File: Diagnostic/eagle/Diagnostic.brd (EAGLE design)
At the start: 90.2 x 80.9 mm, 70 parts, among them J1 S7036-ND, J2 S7036-ND, J3 1175-1864-ND, J4 503182-1852, J5 277-1578-ND, Q1 16 MHz, Q2 16MHz, T2 LD1086D2M33TR, U1 ATMEGA2560AU, U2 BME280, U3 ATMEGA328P-AUR, U4 TXB0108PWR, U5 TPS565208DDCR, U6 TXB0108PWR, X1 B6B-EH-A(LF)(SN), X3 NRF24L01, X5 1751248

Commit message: Working on the board
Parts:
- moved X3 170.1 mm to (44.5, 10.2), turned to 180 degrees
- moved R7 158.3 mm to (73.7, 63.5), turned to 270 degrees
- moved J2 153.0 mm to (87.6, 64.8), turned to 90 degrees
- moved R3 144.5 mm to (71.1, 63.5), turned to 270 degrees
- moved R5 144.0 mm to (64.8, 100.3)
- moved J1 143.1 mm to (87.6, 73.7), turned to 90 degrees
- moved U1 123.9 mm to (47.0, 40.6)
- moved J3 120.9 mm to (83.8, 55.9)
- moved C8 105.4 mm to (59.7, 61.0), turned to 270 degrees
- moved U3 101.4 mm to (73.7, 72.4)
- moved C7 96.8 mm to (59.7, 76.2), turned to 90 degrees
- moved J4 95.6 mm to (10.2, 10.2)
- moved FUSE 89.0 mm to (52.1, 73.7), turned to 180 degrees
- moved U6 86.4 mm to (44.5, 14.0)
- moved C9 85.1 mm to (63.5, 88.9)
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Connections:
- net +3V3: now also C15.1, T2.2
- net +5V: no longer C15.1, T2.2
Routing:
- net LED_RX_5V: track 0.00 -> 73.8 mm, vias 0 -> 2
- net FAN_PWM: track 0.00 -> 69.0 mm
- net LED_TX_5V: track 0.00 -> 68.9 mm, vias 0 -> 2
- net MOSI1_3V3: track 0.00 -> 65.4 mm, vias 0 -> 2
- net ENCODER_SENSE2: track 0.00 -> 65.0 mm, vias 0 -> 1
- net CON_CONNECTED: track 0.00 -> 65.0 mm
- net MISO1_3V3: track 0.00 -> 64.7 mm
- net ENCODER_SENSE1: track 0.00 -> 62.8 mm, vias 0 -> 1
- net +5V_FUSE: track 0.00 -> 52.9 mm, vias 0 -> 1
- net CURRENT_SENSOR: track 0.00 -> 47.2 mm
- net GND: track 20.6 -> 62.0 mm, vias 2 -> 5
- net SS1_5V: track 0.00 -> 38.8 mm, vias 0 -> 2
- net SS2_5V: track 0.00 -> 37.8 mm, vias 0 -> 2
- net RST: track 0.00 -> 36.5 mm, vias 0 -> 2
- net SS0_3V3: track 0.00 -> 31.4 mm
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- added copper zone on layer 1, net +12V
- added copper zone on layer 1, net +3V3
- added copper zone on layer 1, net +5V
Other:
- board size 90.2 x 80.9 mm -> 90.2 x 82.2 mm

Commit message: Finishing touches with board layout
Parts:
- moved C6 171.7 mm to (82.5, 80.0)
- moved C25 170.2 mm to (82.5, 77.5)
- moved C5 161.5 mm to (78.7, 80.0)
- moved C27 159.0 mm to (80.0, 74.9), turned to 90 degrees
- moved Q1 156.2 mm to (69.8, 38.1), turned to 180 degrees
- moved S3 153.7 mm to (66.0, 61.0)
- moved C4 151.4 mm to (74.9, 80.0)
- moved R1 136.4 mm to (78.7, 33.0)
- moved R10 135.5 mm to (19.8, 2.92), turned to 90 degrees
- moved D1 133.6 mm to (48.3, 76.2)
- moved C2 129.2 mm to (73.7, 33.0)
- moved R9 123.3 mm to (64.6, 31.6)
- moved C19 123.1 mm to (59.1, 20.7)
- moved C24 122.1 mm to (38.1, 53.3)
- moved C23 115.3 mm to (38.1, 55.9)
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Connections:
- net LOGIC_RX_3V3: now also U6.3; no longer U4.1
- net LOGIC_RX_5V: now also U6.18; no longer U4.20
- net LOGIC_TX_3V3: now also U6.1; no longer U4.3
- net LOGIC_TX_5V: now also U6.20; no longer U4.18
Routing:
- net GND: track 62.0 -> 144.6 mm, vias 5 -> 24
- net LS_EN: track 0.00 -> 81.1 mm, vias 0 -> 4
- net !RESET1: track 0.00 -> 55.8 mm, vias 0 -> 2
- net N$3: track 0.00 -> 49.0 mm, vias 0 -> 2
- net LOGIC_RX_3V3: track 0.00 -> 45.1 mm
- net RST: track 36.5 -> 79.4 mm
- net LOGIC_TX_3V3: track 0.00 -> 42.2 mm
- net SD_DETECT_3V3: track 0.00 -> 39.7 mm
- net N$2: track 0.00 -> 36.6 mm, vias 0 -> 2
- net CE_3V3: track 0.00 -> 32.8 mm, vias 0 -> 2
- net SD_DETECT_5V: track 0.00 -> 30.8 mm, vias 0 -> 2
- net SCK1_3V3: track 23.8 -> 53.3 mm, vias 0 -> 4
- net +3V3: track 9.86 -> 37.9 mm, vias 4 -> 5
- net IRQ_5V: track 0.00 -> 27.8 mm, vias 0 -> 2
- net CE_5V: track 5.58 -> 29.3 mm
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
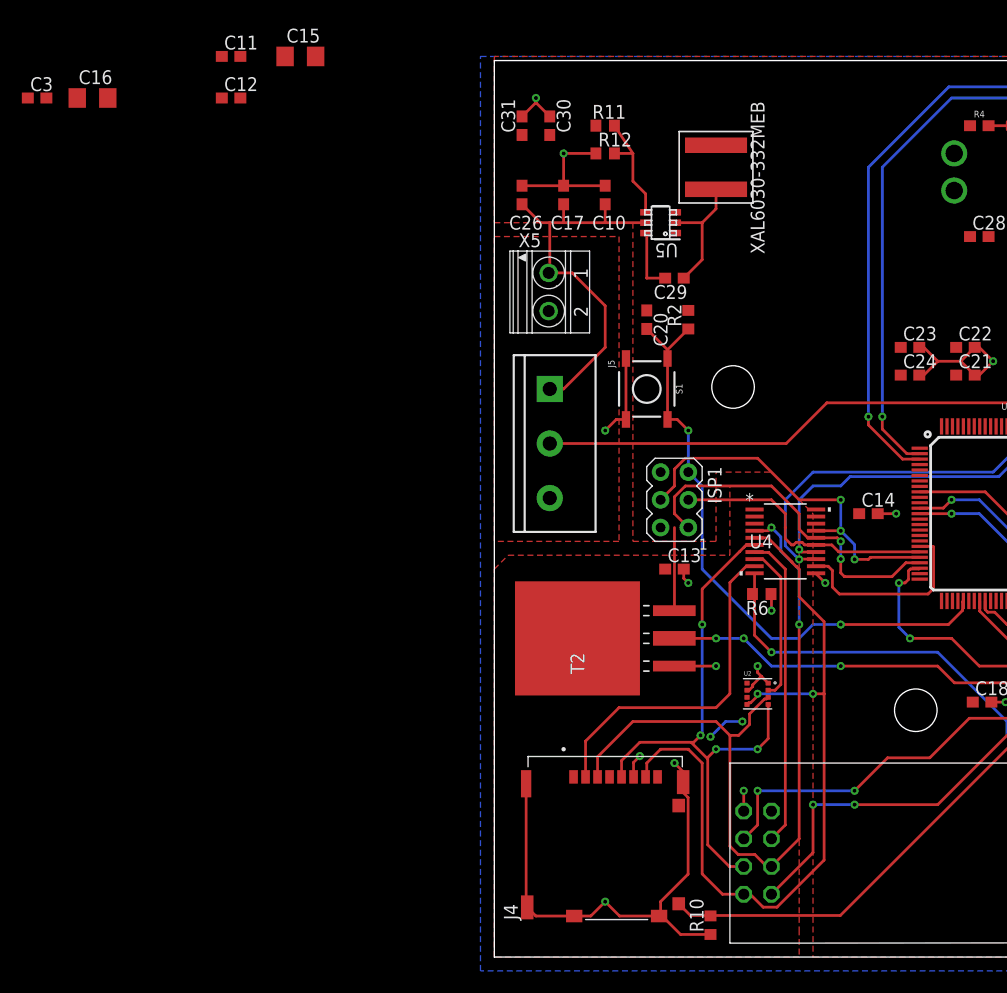
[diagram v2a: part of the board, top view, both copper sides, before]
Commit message: Board functionally done, just need to make it look better
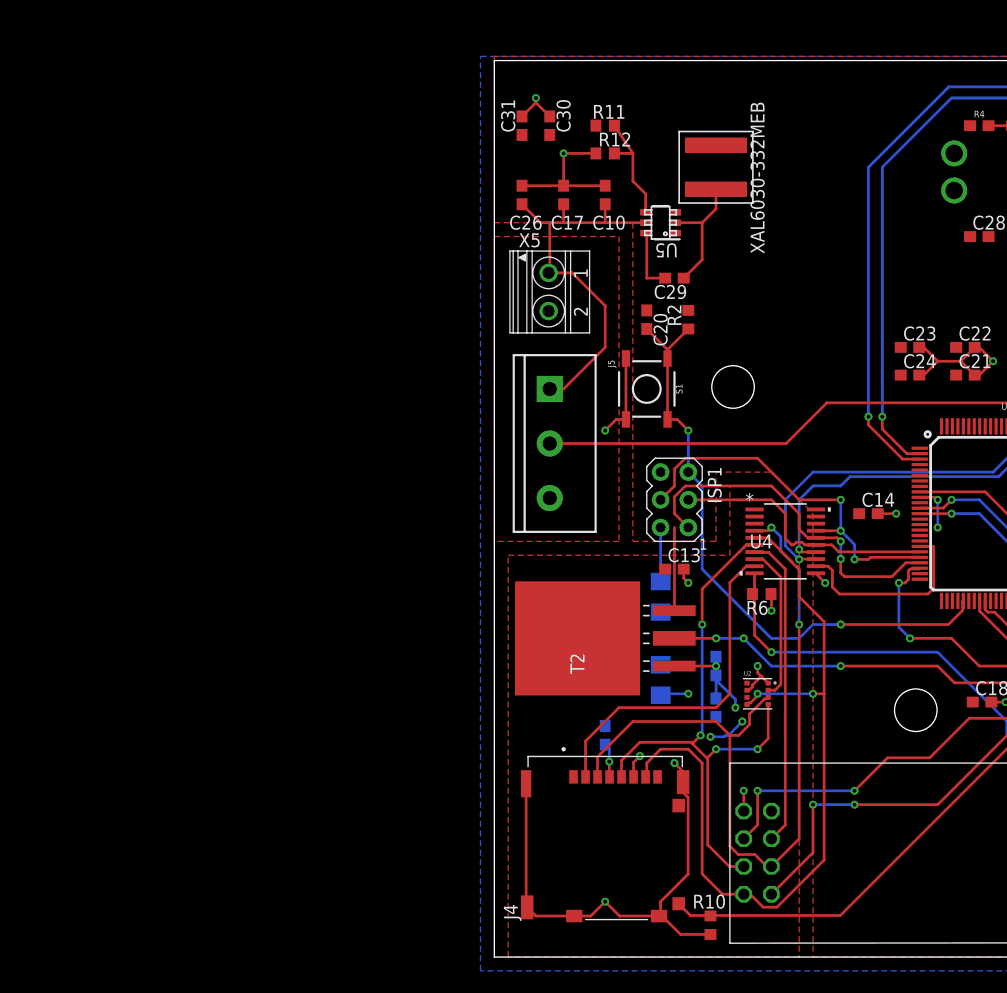
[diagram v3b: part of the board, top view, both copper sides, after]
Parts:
- moved C3 78.3 mm to (10.2, 20.3), flipped to the bottom, turned to 90 degrees
- moved C11 71.4 mm to (20.3, 26.7), flipped to the bottom, turned to 90 degrees
- moved C12 71.4 mm to (20.3, 22.9), flipped to the bottom, turned to 270 degrees
- moved C16 69.3 mm to (15.2, 33.0), flipped to the bottom, turned to 270 degrees
- moved C15 66.0 mm to (15.2, 25.4), flipped to the bottom, turned to 90 degrees
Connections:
- net +3V3: now also C3.1
- net +5V: no longer C3.1
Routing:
- net +3V3: track 37.9 -> 49.0 mm, vias 5 -> 8
- net +5V: track 8.47 -> 17.7 mm, vias 0 -> 2

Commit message: Fixed Airwires
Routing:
- net +5V: track 17.7 -> 51.0 mm, vias 2 -> 4
- net GND: track 144.6 -> 175.4 mm, vias 24 -> 35
- net +5V_FUSE: track 57.1 -> 84.0 mm
- net +3V3: track 49.0 -> 63.9 mm, vias 8 -> 10
- net +12V: track 36.9 -> 40.1 mm
